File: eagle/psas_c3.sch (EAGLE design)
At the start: 41 parts, among them IC1 CP210X_USB_UART, U1 MIC5219 3.3V, Y1 32MHz

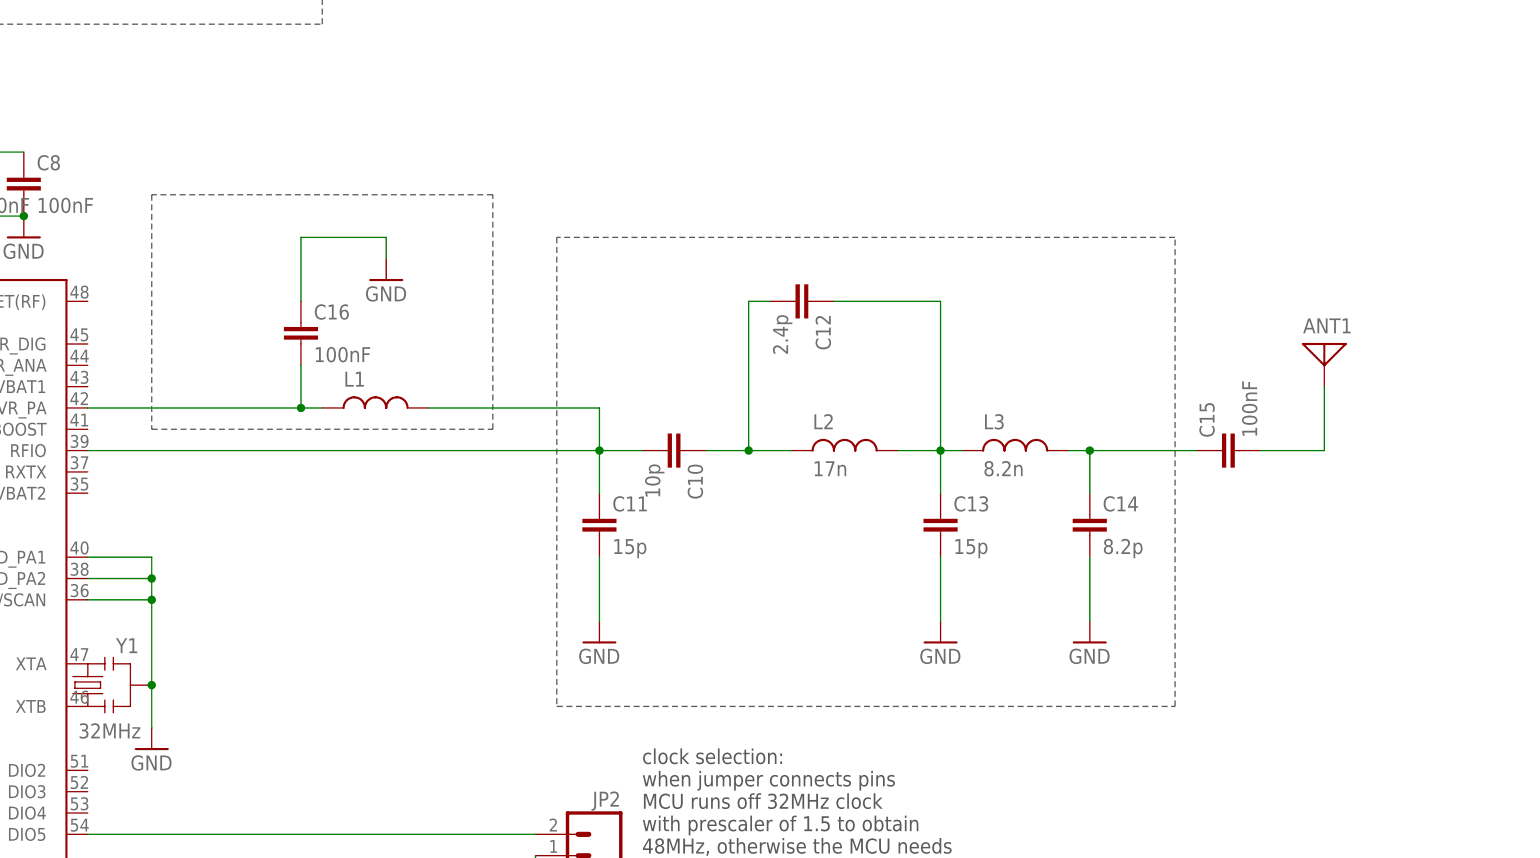
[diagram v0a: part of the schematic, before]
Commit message: Fixed component values to RF circuit. Looks good
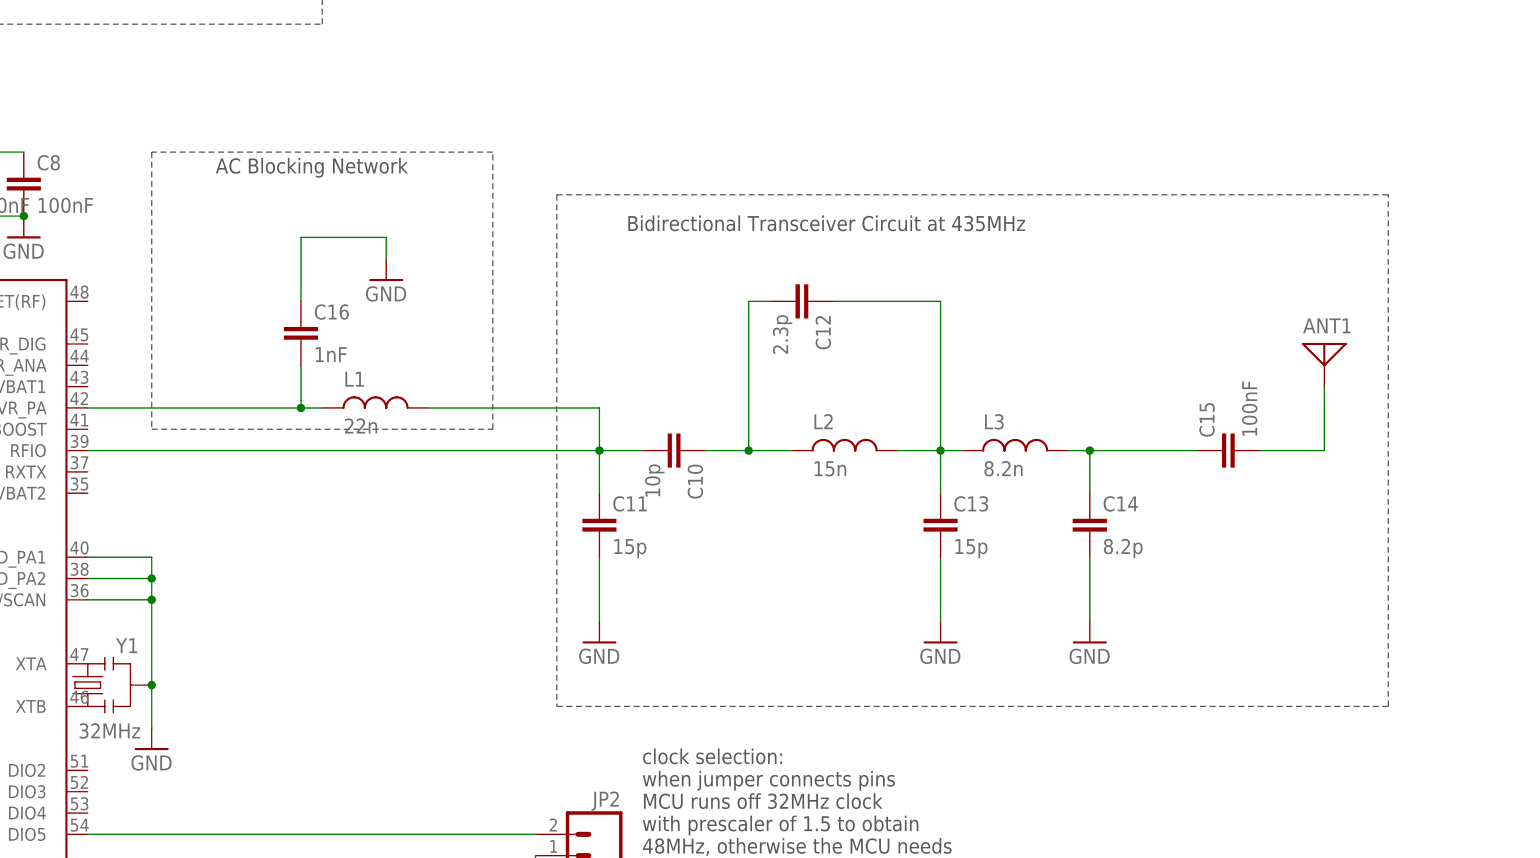
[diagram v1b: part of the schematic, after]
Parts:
- C12: value 2.4p -> 2.3p
- C16: value 100nF -> 1nF
- L1: value (none) -> 22n
- L2: value 17n -> 15n
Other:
- note added: "AC Blocking Network"
- note added: "Bidirectional Transceiver Circuit at 435MHz"
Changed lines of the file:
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@@
 <part name="C10" library="rcl_custom" deviceset="C-EU" device="0603-B-NOSILK" value="10p"/>
 <part name="C11" library="rcl_custom" deviceset="C-EU" device="0603-B-NOSILK" value="15p"/>
-<part name="C12" library="rcl_custom" deviceset="C-EU" device="0603-B-NOSILK" value="2.4p"/>
+<part name="C12" library="rcl_custom" deviceset="C-EU" device="0603-B-NOSILK" value="2.3p"/>
 <part name="C13" library="rcl_custom" deviceset="C-EU" device="0603-B-NOSILK" value="15p"/>
 <part name="C14" library="rcl_custom" deviceset="C-EU" device="0603-B-NOSILK" value="8.2p"/>
@@
 <part name="GND19" library="Vibrogait_prototype" deviceset="GND" device=""/>
 <part name="C15" library="rcl_custom" deviceset="C-EU" device="0603-B-NOSILK" value="100nF"/>
-<part name="C16" library="rcl_custom" deviceset="C-EU" device="0603-B-NOSILK" value="100nF"/>
+<part name="C16" library="rcl_custom" deviceset="C-EU" device="0603-B-NOSILK" value="1nF"/>
 <part name="GND20" library="Vibrogait_prototype" deviceset="GND" device=""/>
 <part name="ANT1" library="discrete" deviceset="ANTENNA" device=""/>
-<part name="L1" library="rcl_custom" deviceset="L-US" device="0603-B-NOSILK"/>
-<part name="L2" library="rcl_custom" deviceset="L-US" device="0603-B-NOSILK" value="17n"/>
+<part name="L1" library="rcl_custom" deviceset="L-US" device="0603-B-NOSILK" value="22n"/>
+<part name="L2" library="rcl_custom" deviceset="L-US" device="0603-B-NOSILK" value="15n"/>
 <part name="L3" library="rcl_custom" deviceset="L-US" device="0603-B-NOSILK" value="8.2n"/>
 <part name="GND21" library="Vibrogait_prototype" deviceset="GND" device=""/>
@@
 to run off internal clock reference
 (see datasheet for details)</text>
-<wire x1="119.38" y1="134.62" x2="119.38" y2="106.68" width="0.1524" layer="97" style="dashdot"/>
+<wire x1="119.38" y1="139.7" x2="119.38" y2="106.68" width="0.1524" layer="97" style="dashdot"/>
 <wire x1="119.38" y1="106.68" x2="160.02" y2="106.68" width="0.1524" layer="97" style="dashdot"/>
-<wire x1="160.02" y1="106.68" x2="160.02" y2="134.62" width="0.1524" layer="97" style="dashdot"/>
-<wire x1="160.02" y1="134.62" x2="119.38" y2="134.62" width="0.1524" layer="97" style="dashdot"/>
-<wire x1="167.64" y1="129.54" x2="167.64" y2="73.66" width="0.1524" layer="97" style="dashdot"/>
-<wire x1="167.64" y1="73.66" x2="241.3" y2="73.66" width="0.1524" layer="97" style="dashdot"/>
-<wire x1="241.3" y1="73.66" x2="241.3" y2="129.54" width="0.1524" layer="97" style="dashdot"/>
-<wire x1="241.3" y1="129.54" x2="167.64" y2="129.54" width="0.1524" layer="97" style="dashdot"/>
+<wire x1="160.02" y1="106.68" x2="160.02" y2="139.7" width="0.1524" layer="97" style="dashdot"/>
+<wire x1="160.02" y1="139.7" x2="119.38" y2="139.7" width="0.1524" layer="97" style="dashdot"/>
+<wire x1="167.64" y1="134.62" x2="167.64" y2="73.66" width="0.1524" layer="97" style="dashdot"/>
+<wire x1="167.64" y1="73.66" x2="266.7" y2="73.66" width="0.1524" layer="97" style="dashdot"/>
+<wire x1="266.7" y1="73.66" x2="266.7" y2="134.62" width="0.1524" layer="97" style="dashdot"/>
+<wire x1="266.7" y1="134.62" x2="167.64" y2="134.62" width="0.1524" layer="97" style="dashdot"/>
+<text x="127" y="137.16" size="1.778" layer="97">AC Blocking Network</text>
+<text x="223.52" y="132.08" size="1.778" layer="97" rot="R180">Bidirectional Transceiver Circuit at 435MHz</text>
 </plain>
 <instances>

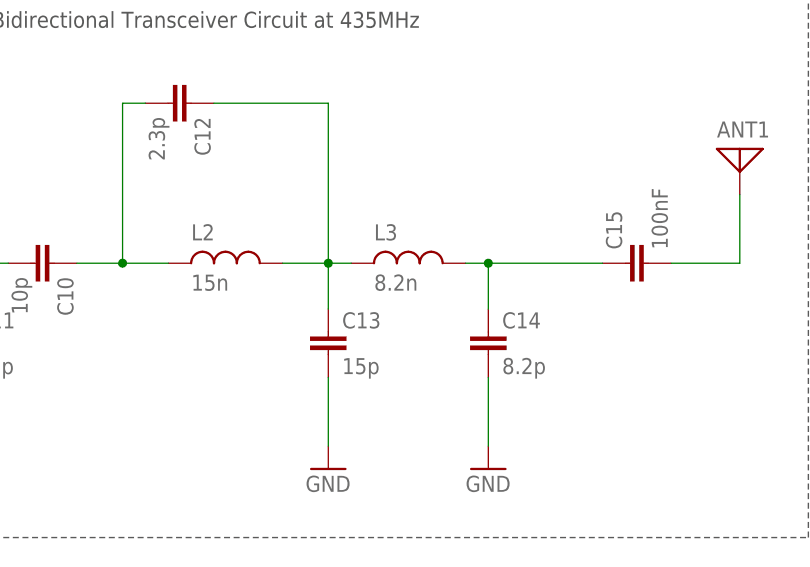
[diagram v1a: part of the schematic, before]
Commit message: Fixed one component value (inductor)
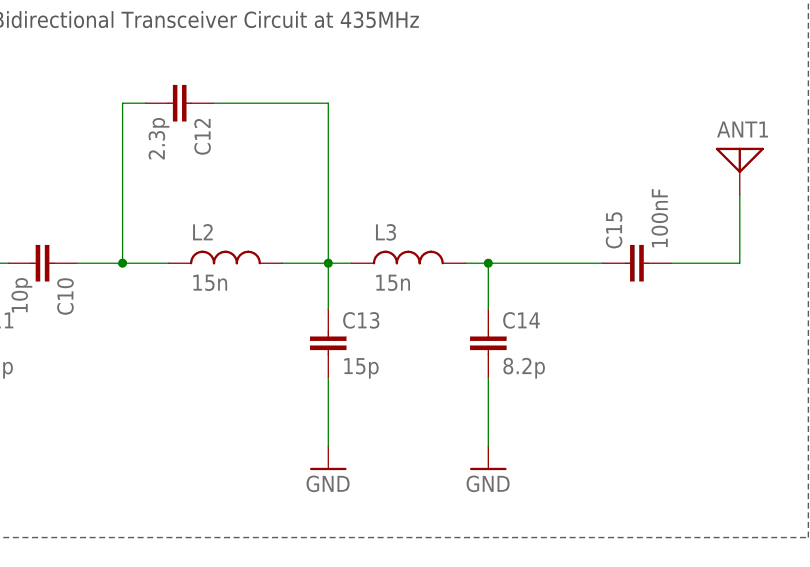
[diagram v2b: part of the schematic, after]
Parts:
- L3: value 8.2n -> 15n
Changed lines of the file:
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@@
 <part name="L1" library="rcl_custom" deviceset="L-US" device="0603-B-NOSILK" value="22n"/>
 <part name="L2" library="rcl_custom" deviceset="L-US" device="0603-B-NOSILK" value="15n"/>
-<part name="L3" library="rcl_custom" deviceset="L-US" device="0603-B-NOSILK" value="8.2n"/>
+<part name="L3" library="rcl_custom" deviceset="L-US" device="0603-B-NOSILK" value="15n"/>
 <part name="GND21" library="Vibrogait_prototype" deviceset="GND" device=""/>
 <part name="JP3" library="pinhead" deviceset="PINHD-1X2" device=""/>

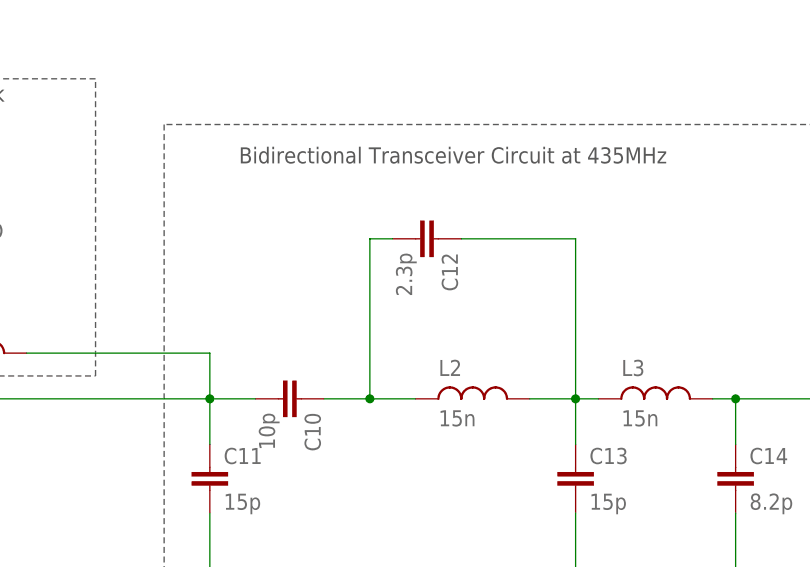
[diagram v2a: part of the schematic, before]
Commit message: Added a RF folder for all RF materials and changed another component value
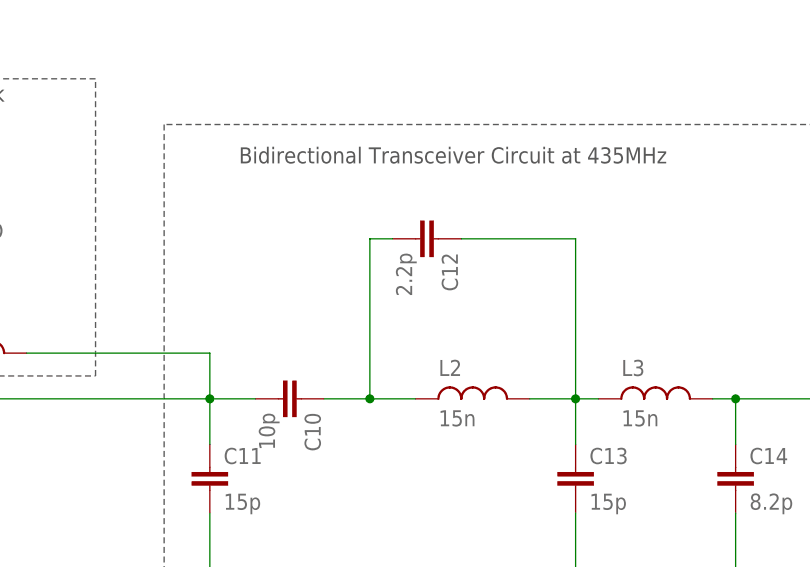
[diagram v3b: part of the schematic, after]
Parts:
- C12: value 2.3p -> 2.2p
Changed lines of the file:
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@@
 <?xml version="1.0" encoding="utf-8"?>
 <!DOCTYPE eagle SYSTEM "eagle.dtd">
-<eagle version="6.3">
+<eagle version="7.4.0">
 <drawing>
 <settings>
@@
 <part name="C10" library="rcl_custom" deviceset="C-EU" device="0603-B-NOSILK" value="10p"/>
 <part name="C11" library="rcl_custom" deviceset="C-EU" device="0603-B-NOSILK" value="15p"/>
-<part name="C12" library="rcl_custom" deviceset="C-EU" device="0603-B-NOSILK" value="2.3p"/>
+<part name="C12" library="rcl_custom" deviceset="C-EU" device="0603-B-NOSILK" value="2.2p"/>
 <part name="C13" library="rcl_custom" deviceset="C-EU" device="0603-B-NOSILK" value="15p"/>
 <part name="C14" library="rcl_custom" deviceset="C-EU" device="0603-B-NOSILK" value="8.2p"/>

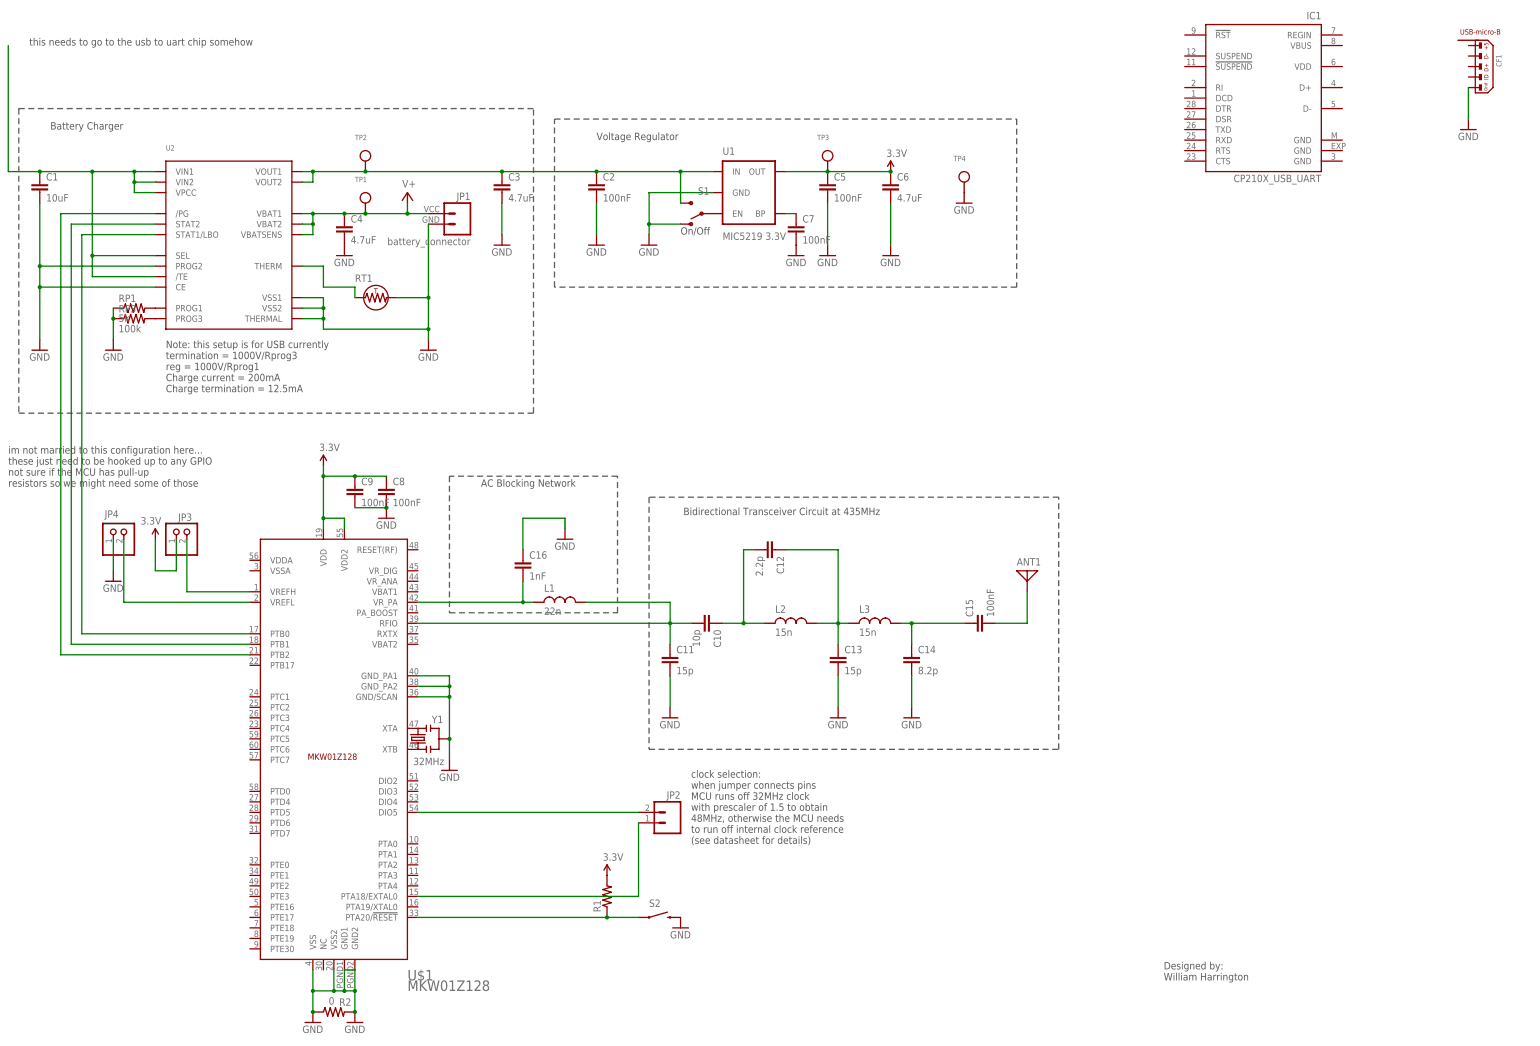
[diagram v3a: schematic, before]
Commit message: Added the USB to UART chip
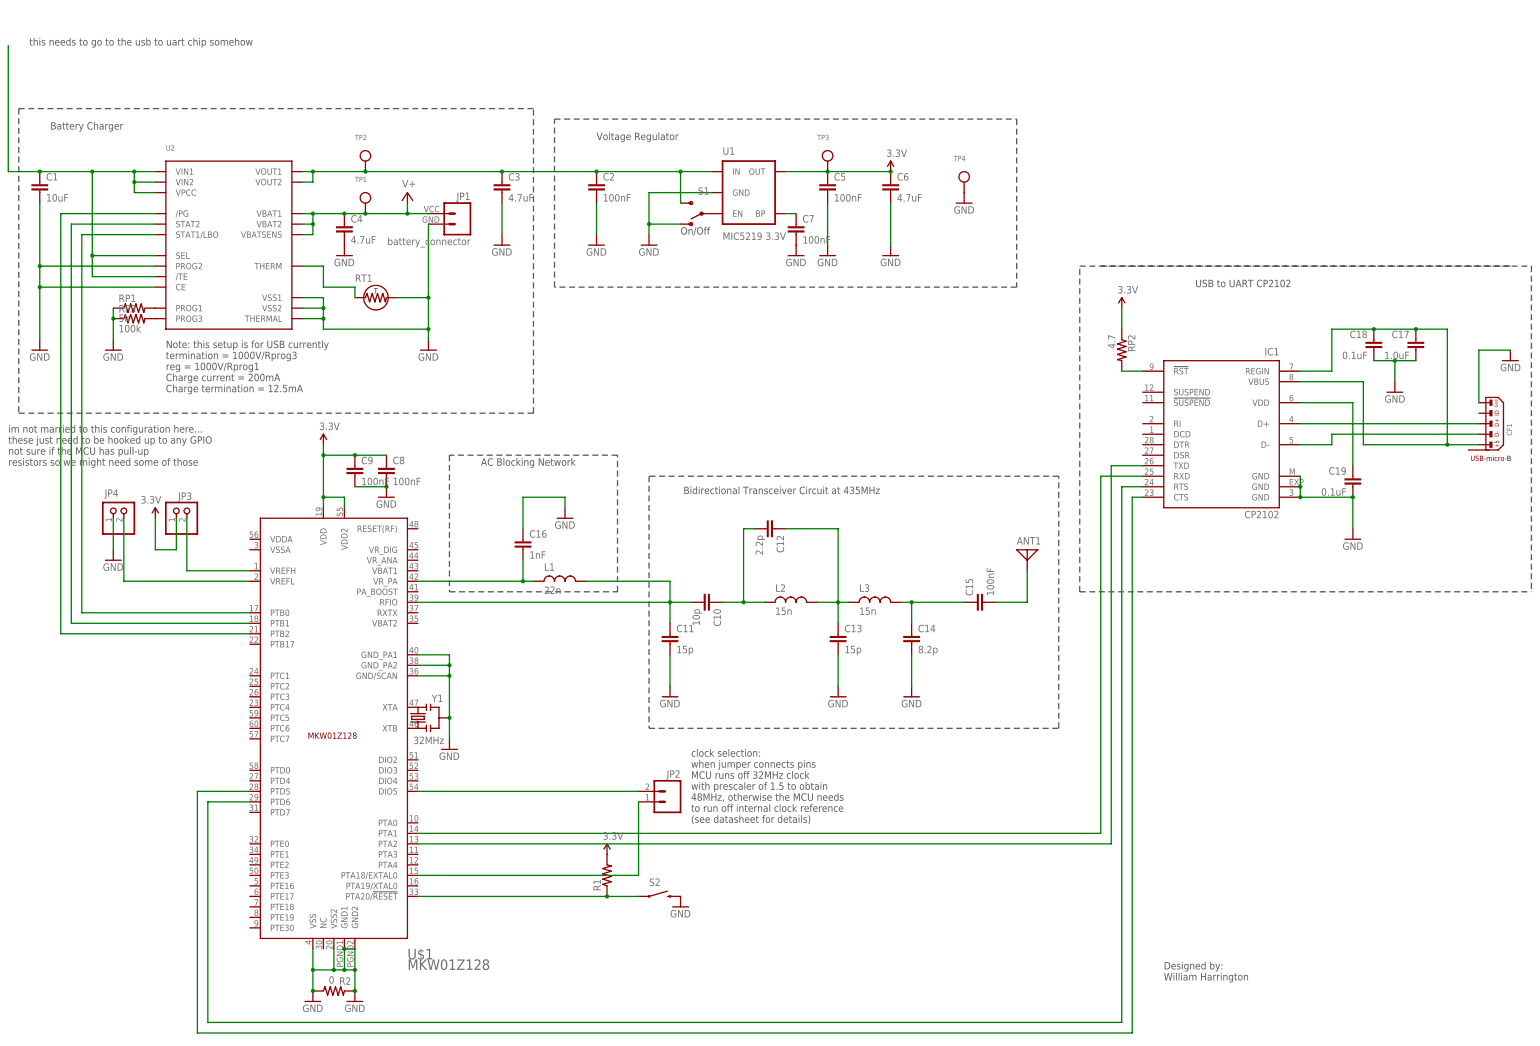
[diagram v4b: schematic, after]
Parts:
- added C17: 1.0uF, rcl_custom:C-EU0603-B-NOSILK
- added C18, C19: 0.1uF, rcl_custom:C-EU0603-B-NOSILK
- added RP2: 4.7, rcl_custom:R-US_0603-B-NOSILK
- IC1: value CP210X_USB_UART -> CP2102; device SparkFun-v5:CP210X_USB_UART -> silabs:CP2102; DIST Digi-Key -> (none); DPN 336-1162-ND -> (none); MFG Silicon Labs -> (none); MPN CP2101-GM -> (none)
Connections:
- new net N$25: CF1.3, IC1.D+
- new net N$26: C17.1, C18.1, CF1.1, IC1.REGIN, IC1.VBUS
- new net N$27: C19.1, IC1.VDD
- new net N$28: IC1.RXD, U$1.PTA1
- new net N$29: IC1.TXD, U$1.PTA2
- new net N$30: IC1.!RST, RP2.2
- new net N$31: CF1.2, IC1.D-
- new net N$32: IC1.RTS, U$1.PTD6
- new net N$33: IC1.CTS, U$1.PTD5
- net 3.3V: now also RP2.1
- net GND: now also C17.2, C18.2, C19.2, IC1.GND, IC1.GND@EXP, IC1.GND@M, U$1.GND1
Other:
- note added: "USB to UART CP2102"
- moved on the sheet: ANT1, C10, C11, C12, C13, C14, C15, C16, C8, C9, CF1, IC1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
